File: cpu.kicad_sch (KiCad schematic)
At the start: 9 parts, among them J2 USB4105-GF-A

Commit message: Modofied power flags and other minor edits.
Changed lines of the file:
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@@
     (stroke (width 0) (type default))
   )
-  (wire (pts (xy 200.025 49.53) (xy 200.025 48.26))
+  (wire (pts (xy 192.405 45.72) (xy 192.405 49.53))
+    (stroke (width 0) (type default))
+  )
+  (wire (pts (xy 200.025 49.53) (xy 200.025 45.72))
     (stroke (width 0) (type default))
   )
@@
   )
   (wire (pts (xy 68.58 102.235) (xy 97.79 102.235))
+    (stroke (width 0) (type default))
+  )
+  (wire (pts (xy 192.405 49.53) (xy 200.025 49.53))
     (stroke (width 0) (type default))
   )
@@
         (path "/7aab8e99-eed8-4c64-b2cd-ed9d372ca98a"
           (reference "#PWR044") (unit 1)
+        )
+      )
+    )
+  )
+  (symbol (lib_id "power:PWR_FLAG") (at 192.405 45.72 0) (unit 1)
+    (in_bom yes) (on_board yes) (dnp no)
+    (property "Reference" "#FLG03" (at 192.405 43.815 0)
+      (effects (font (size 1 1)) hide)
+    )
+    (property "Value" "PWR_FLAG" (at 192.405 41.91 0)
+      (effects (font (size 1 1)))
+    )
+    (property "Footprint" "" (at 192.405 45.72 0)
+      (effects (font (size 1 1)) hide)
+    )
+    (property "Datasheet" "~" (at 192.405 45.72 0)
+      (effects (font (size 1 1)) hide)
+    )
+    (pin "1")
+    (instances
+      (project "cpu"
+        (path "/7aab8e99-eed8-4c64-b2cd-ed9d372ca98a"
+          (reference "#FLG03") (unit 1)
         )
       )
@@
     )
   )
-  (symbol (lib_id "power:+5V") (at 200.025 48.26 0) (unit 1)
-    (in_bom yes) (on_board yes) (dnp no)
-    (property "Reference" "#PWR042" (at 200.025 52.07 0)
-      (effects (font (size 1 1)) hide)
-    )
-    (property "Value" "+5V" (at 200.406 43.8658 0)
-      (effects (font (size 1 1)))
-    )
-    (property "Footprint" "" (at 200.025 48.26 0)
-      (effects (font (size 1 1)) hide)
-    )
-    (property "Datasheet" "" (at 200.025 48.26 0)
-      (effects (font (size 1 1)) hide)
-    )
+  (symbol (lib_id "power:+5V") (at 200.025 45.72 0) (unit 1)
+    (in_bom yes) (on_board yes) (dnp no)
+    (property "Reference" "#PWR042" (at 200.025 49.53 0)
+      (effects (font (size 1 1)) hide)
+    )
+    (property "Value" "+5V" (at 200.025 41.91 0)
+      (effects (font (size 1 1)))
+    )
+    (property "Footprint" "" (at 200.025 45.72 0)
+      (effects (font (size 1 1)) hide)
+    )
+    (property "Datasheet" "" (at 200.025 45.72 0)
+      (effects (font (size 1 1)) hide)
+    )

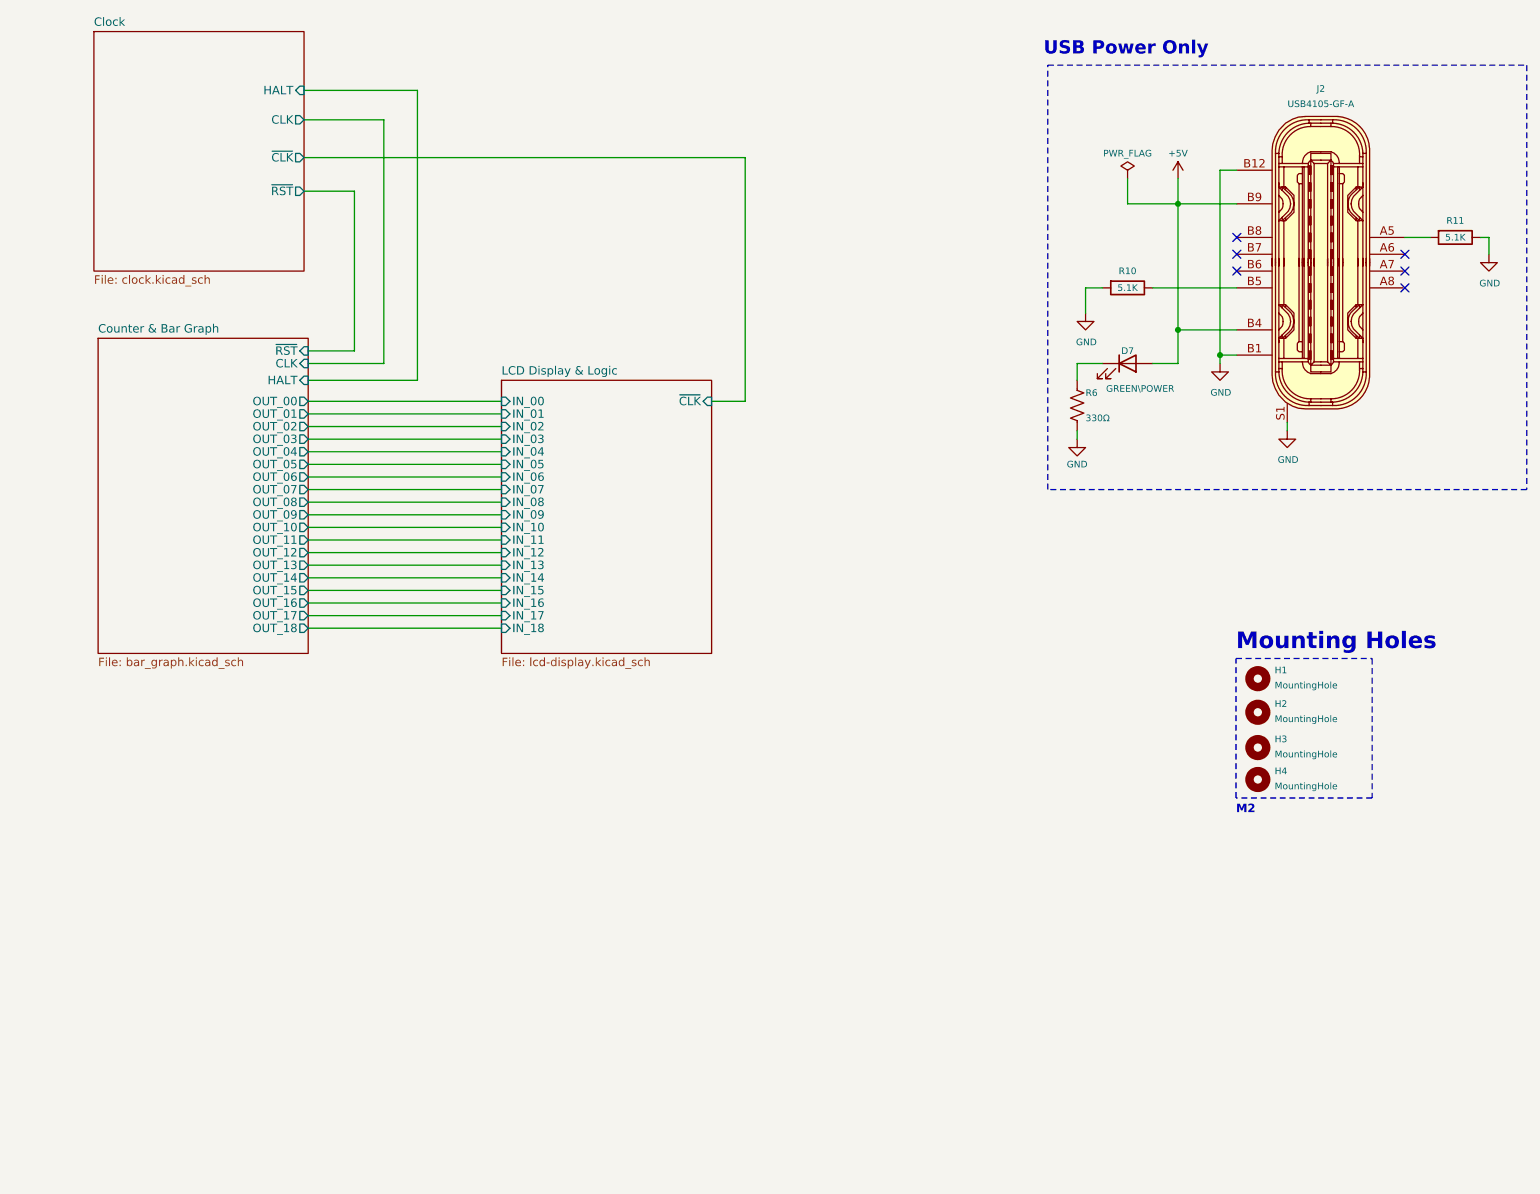
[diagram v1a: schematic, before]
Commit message: Changed out USB connector for new power-only version with fewer pins. Generated new gerber/drill files.
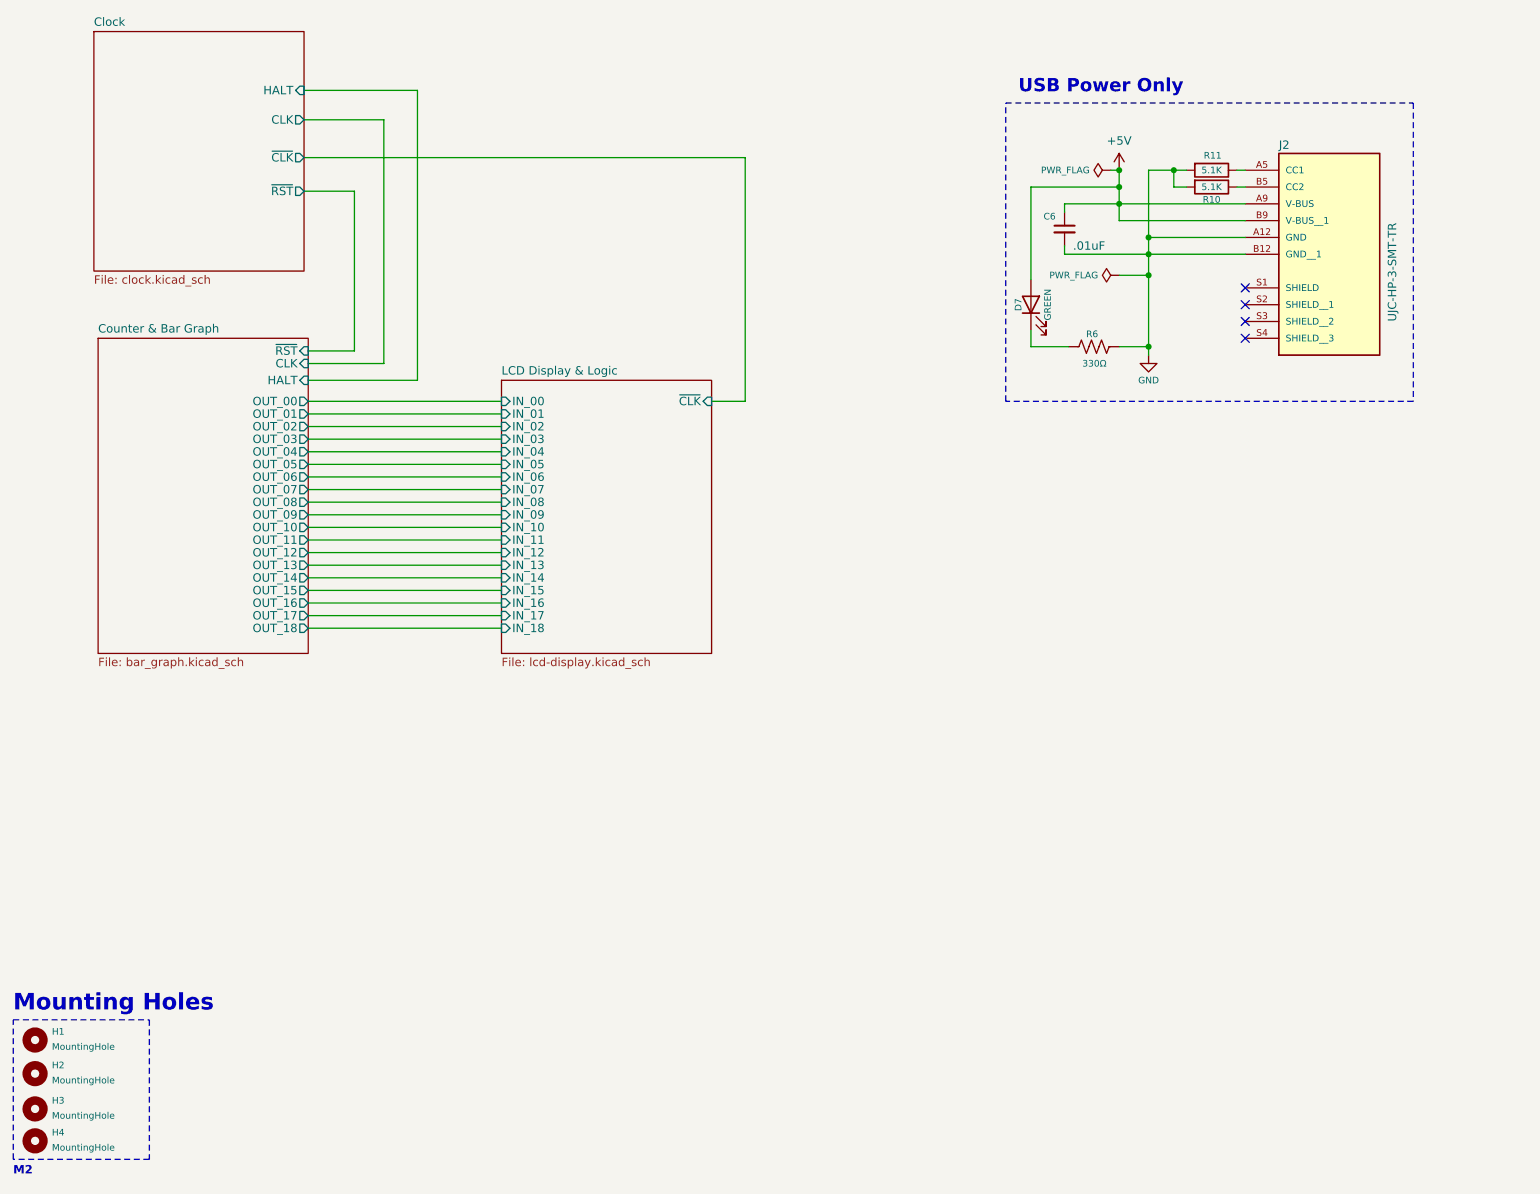
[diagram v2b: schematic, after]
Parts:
- removed J2: USB4105-GF-A, footprints:USB_C_Receptacle_HRO_TYPE-C-31-M-12, symbol homebrew_cpu:USB4105-GF-A
- added C6: .01uF, Capacitor_THT:C_Disc_D4.7mm_W2.5mm_P5.00mm, symbol Device:C_Small
- added J2: UJC-HP-3-SMT-TR, footprints:CUI_UJC-HP-3-SMT-TR, symbol homebrew_cpu:UJC-HP-3-SMT-TR
- D7: value GREEN\POWER -> GREEN
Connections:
- net +5V: now also C6.1, J2.A9 (V-BUS), J2.B9 (V-BUS__1)
- net GND: now also R11.2, C6.2, J2.A12 (GND), J2.B12 (GND__1); no longer R11.1
- net at R10.1: now also J2.B5 (CC2)
- new net: J2.A5 (CC1), R11.1
- no-connect marks 6 -> 4
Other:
- moved on the sheet: H1, H2, H3, H4

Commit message: Updated symbols/footprint for USB and 5K Trimmer Pots.
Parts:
- J2: footprint footprints:CUI_UJC-HP-3-SMT-TR -> footprints:CUI_UJC-HP-M-G-5-MSMT-TR; symbol homebrew_cpu:UJC-HP-3-SMT-TR -> homebrew_cpu:CUI_UJC-HP-M-G-5-MSMT-TR
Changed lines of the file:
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@@
     )
   )
-  (symbol (lib_id "homebrew_cpu:UJC-HP-3-SMT-TR") (at 222.885 49.53 0) (unit 1)
+  (symbol (lib_id "homebrew_cpu:CUI_UJC-HP-M-G-5-MSMT-TR") (at 222.885 49.53 0) (unit 1)
     (in_bom yes) (on_board yes) (dnp no)
     (property "Reference" "J2" (at 215.265 40.64 0)
@@
       (effects (font (size 1.27 1.27)) (justify left))
     )
-    (property "Footprint" "footprints:CUI_UJC-HP-3-SMT-TR" (at 222.885 49.53 0)
+    (property "Footprint" "footprints:CUI_UJC-HP-M-G-5-MSMT-TR" (at 222.885 49.53 0)
       (effects (font (size 1.27 1.27)) (justify bottom) hide)
     )

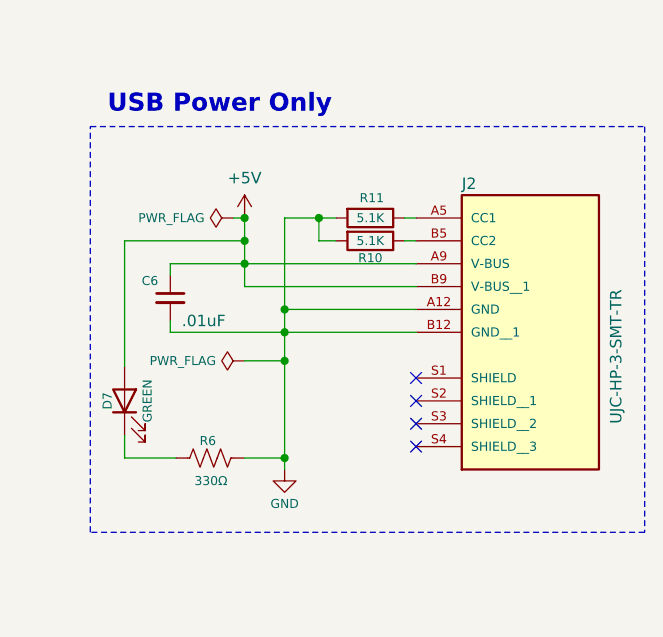
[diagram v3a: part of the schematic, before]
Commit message: Final changes around adding BOM to README.md
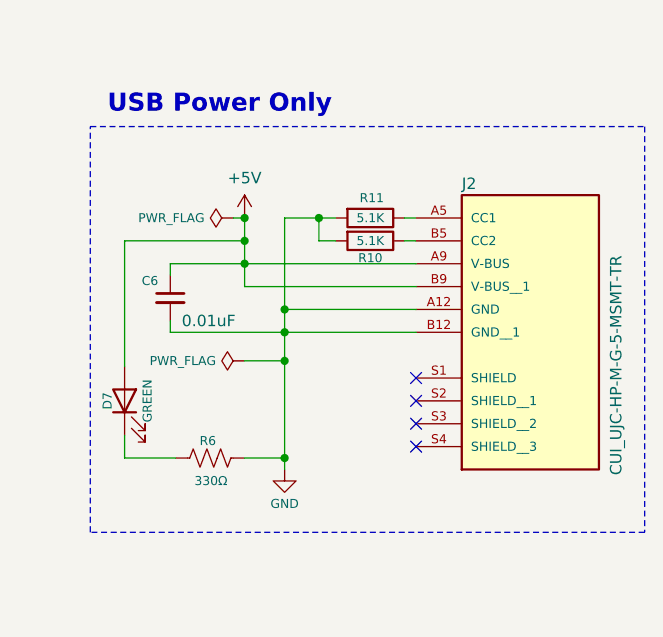
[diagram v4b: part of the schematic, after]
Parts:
- C6: value .01uF -> 0.01uF
- H1, H2, H3, H4: now left out of the parts list
- J2: value UJC-HP-3-SMT-TR -> CUI_UJC-HP-M-G-5-MSMT-TR
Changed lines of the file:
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@@
   )
   (symbol (lib_id "Mechanical:MountingHole") (at 27.305 180.975 0) (unit 1)
-    (in_bom yes) (on_board yes) (dnp no)
+    (in_bom no) (on_board yes) (dnp no)
     (property "Reference" "H2" (at 29.845 179.705 0)
       (effects (font (size 1 1)) (justify left))
@@
       (effects (font (size 1 1)) hide)
     )
+    (property "Sim.Enable" "0" (at 27.305 180.975 0)
+      (effects (font (size 1.27 1.27)) hide)
+    )
     (instances
       (project "cpu"
@@
   )
   (symbol (lib_id "Mechanical:MountingHole") (at 27.305 191.135 0) (unit 1)
-    (in_bom yes) (on_board yes) (dnp no)
+    (in_bom no) (on_board yes) (dnp no)
     (property "Reference" "H4" (at 29.845 189.865 0)
       (effects (font (size 1 1)) (justify left))
@@
       (effects (font (size 1 1)) hide)
     )
+    (property "Sim.Enable" "0" (at 27.305 191.135 0)
+      (effects (font (size 1.27 1.27)) hide)
+    )
     (instances
       (project "cpu"
@@
       (effects (font (size 1 1)) (justify left))
     )
-    (property "Value" ".01uF" (at 184.15 55.88 0)
+    (property "Value" "0.01uF" (at 184.15 55.88 0)
       (effects (font (size 1.27 1.27)) (justify left))
     )
@@
       (effects (font (size 1.27 1.27)) (justify left))
     )
-    (property "Value" "UJC-HP-3-SMT-TR" (at 232.41 67.31 90)
+    (property "Value" "CUI_UJC-HP-M-G-5-MSMT-TR" (at 232.41 73.025 90)
       (effects (font (size 1.27 1.27)) (justify left))
     )
@@
   )
   (symbol (lib_id "Mechanical:MountingHole") (at 27.305 186.309 0) (unit 1)
-    (in_bom yes) (on_board yes) (dnp no)
+    (in_bom no) (on_board yes) (dnp no)
     (property "Reference" "H3" (at 29.845 185.039 0)
       (effects (font (size 1 1)) (justify left))
@@
     (property "Datasheet" "~" (at 27.305 186.309 0)
       (effects (font (size 1 1)) hide)
+    )
+    (property "Sim.Enable" "0" (at 27.305 186.309 0)
+      (effects (font (size 1.27 1.27)) hide)
     )
     (instances
@@
   )
   (symbol (lib_id "Mechanical:MountingHole") (at 27.305 175.895 0) (unit 1)
-    (in_bom yes) (on_board yes) (dnp no)
+    (in_bom no) (on_board yes) (dnp no)
     (property "Reference" "H1" (at 29.845 174.625 0)
       (effects (font (size 1 1)) (justify left))
@@
       (effects (font (size 1 1)) hide)
     )
-    (instances
+    (property "Sim.Enable" "0" (at 27.305 175.895 0)
+      (effects (font (size 1.27 1.27)) hide)
+    )
+    (instances

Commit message: V1.1-last Kicad v7 version
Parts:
- J2: footprint footprints:CUI_UJC-HP-M-G-5-MSMT-TR -> Homebrew-CPU-PCB:CUI_UJC-HP-M-G-5-MSMT-TR; symbol homebrew_cpu:CUI_UJC-HP-M-G-5-MSMT-TR -> Homebrew-CPU-PCB:CUI_UJC-HP-M-G-5-MSMT-TR
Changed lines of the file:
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@@
     )
   )
-  (symbol (lib_id "homebrew_cpu:CUI_UJC-HP-M-G-5-MSMT-TR") (at 222.885 49.53 0) (unit 1)
+  (symbol (lib_id "Homebrew-CPU-PCB:CUI_UJC-HP-M-G-5-MSMT-TR") (at 222.885 49.53 0) (unit 1)
     (in_bom yes) (on_board yes) (dnp no)
     (property "Reference" "J2" (at 215.265 40.64 0)
@@
       (effects (font (size 1.27 1.27)) (justify left))
     )
-    (property "Footprint" "footprints:CUI_UJC-HP-M-G-5-MSMT-TR" (at 222.885 49.53 0)
+    (property "Footprint" "Homebrew-CPU-PCB:CUI_UJC-HP-M-G-5-MSMT-TR" (at 222.885 49.53 0)
       (effects (font (size 1.27 1.27)) (justify bottom) hide)
     )
